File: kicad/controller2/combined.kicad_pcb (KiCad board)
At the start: 2 copper layers, 150.5 x 97.2 mm, 258 parts, among them J1 Conn_01x07_Male, J2 Conn_01x07_Male, J3 Conn_01x07_Male, J4 Conn_01x07_Male, J5V1 Conn_01x01_Male, Q1 BC846B, Q2 IRF3205, Q3 IRF3205, Q4 BC846B, Q5 IRF3205, Q6 IRF3205, U1 BluePill_STM32F103C, U1 LM324, U2 LM324

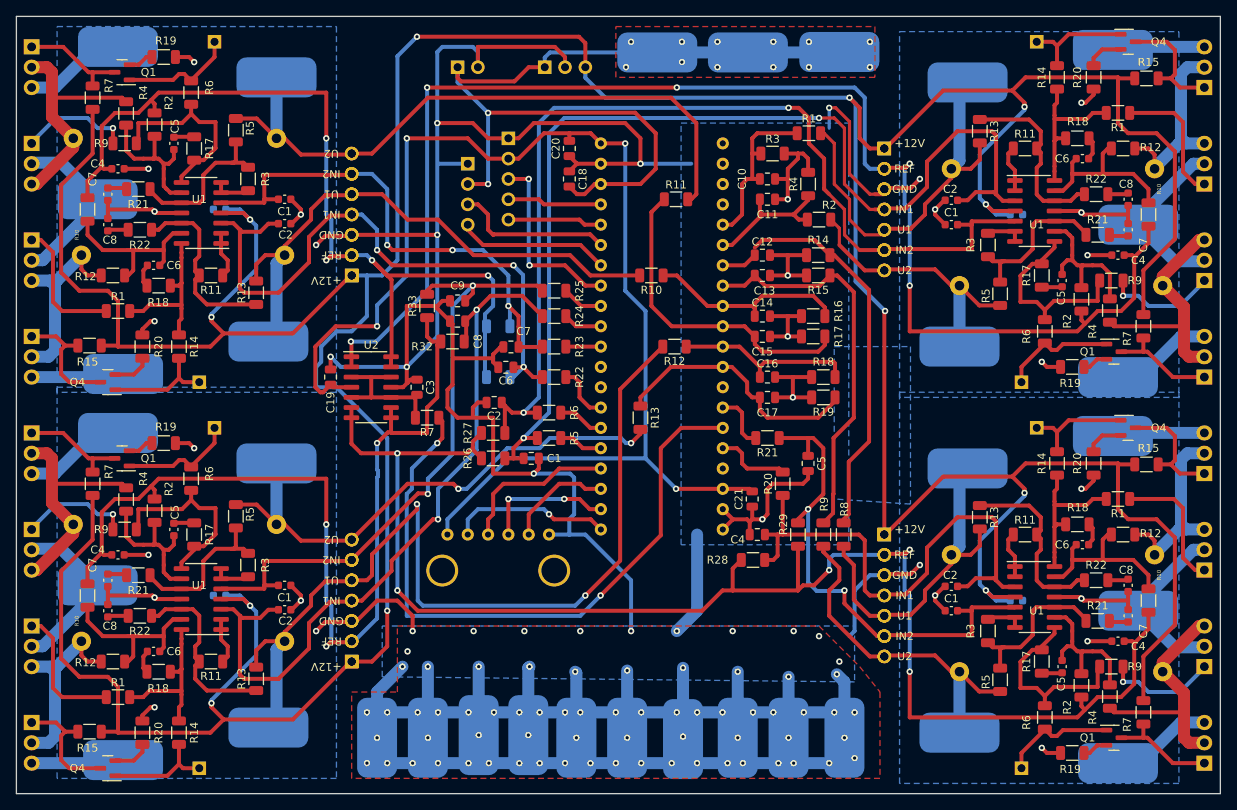
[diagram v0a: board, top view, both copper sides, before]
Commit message: minor schematic cleanups, improve opamp compensation
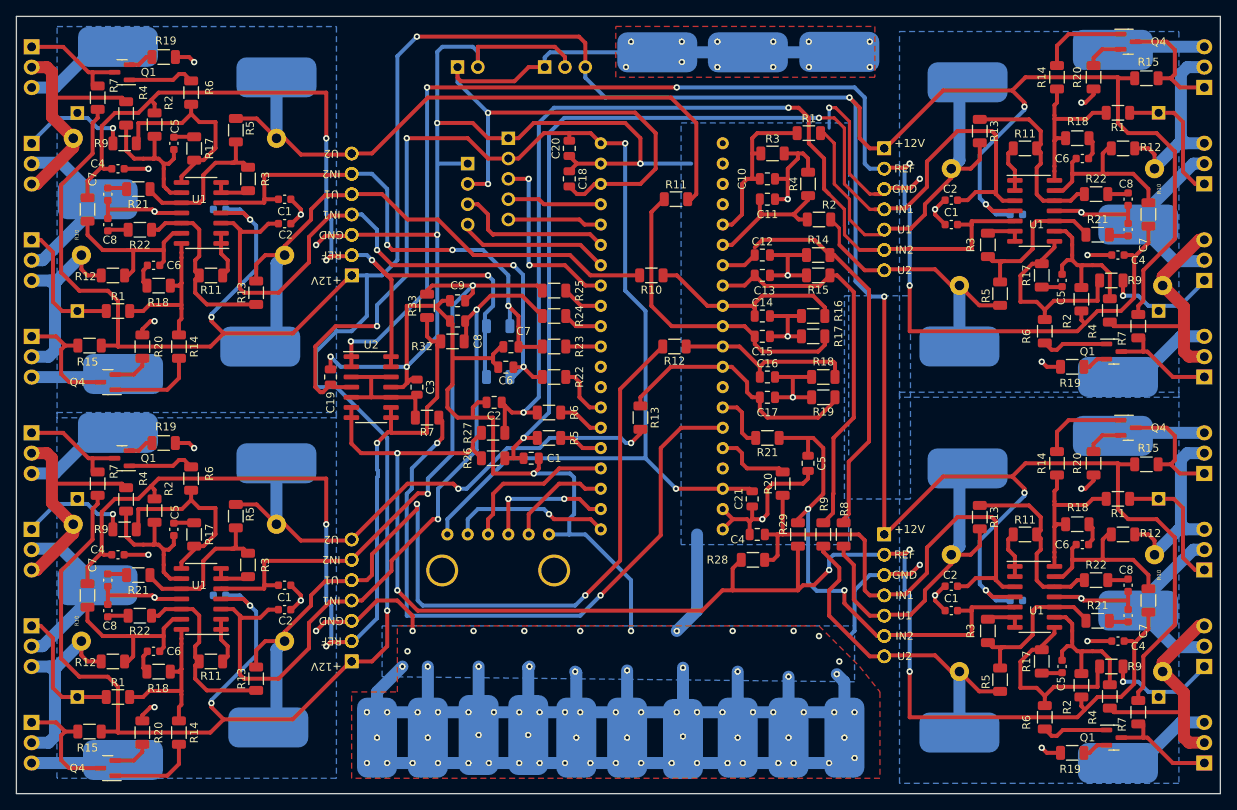
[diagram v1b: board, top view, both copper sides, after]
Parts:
- removed the C1 at (195.0, 120.0)
- removed the C1 at (195.0, 71.8)
- removed the C1 at (142.5, 101.0)
- removed the C1 at (111.6, 116.8)
- removed the C2 at (195.0, 117.0)
- removed the C2 at (137.8, 94.0)
- removed the C2 at (111.6, 119.9)
- removed the C2 at (195.0, 68.7)
- removed the C3 at (128.2, 92.1)
- removed the C3 at (203.1, 70.5)
- removed the C3 at (103.5, 118.1)
- removed the C3 at (203.1, 118.7)
- removed the C4 at (215.8, 75.6)
- removed the C4 at (90.8, 113.0)
- removed the C4 at (170.7, 110.5)
- removed the C4 at (215.8, 123.8)
- removed the C5 at (97.8, 109.9)
- removed the C5 at (208.8, 78.7)
- removed the C5 at (208.8, 127.0)
- removed the C5 at (177.1, 101.6)
- removed the C6 at (139.3, 89.6)
- removed the C6 at (211.4, 63.5)
- removed the C6 at (211.4, 111.8)
- removed the C6 at (95.2, 125.1)
- removed the C7 at (139.9, 87.0)
- removed the C7 at (217.1, 120.6)
- removed the C7 at (217.1, 72.4)
- removed the C7 at (89.5, 116.2)
- removed the C8 at (217.1, 116.8)
- removed the C8 at (89.5, 120.0)
- removed the C8 at (217.1, 68.6)
- removed the C8 at (133.3, 83.8)
- removed the J1 at (186.6, 110.5)
- removed the J1 at (186.6, 62.2) (x2)
- removed the J1 at (120.0, 126.4)
- removed the J5V1 at (218.3, 120.0)
- removed the J5V1 at (88.3, 116.8)
- removed the J5V1 at (218.3, 71.8)
- removed the JBat1 at (109.6, 134.6)
- removed the JBat1 at (109.6, 86.4)
- removed the JBat1 at (197.0, 54.0)
- removed the JBat1 at (197.0, 102.2)
- removed the JBat1 at (127.0, 130.8)
- removed the JBat2 at (196.0, 135.2)
- removed the JBat2 at (196.0, 87.0)
- removed the JBat2 at (110.6, 101.6)
- removed the JBat2 at (138.4, 140.6)
- removed the JGND1 at (215.2, 98.2)
- removed the JGND1 at (215.2, 49.9)
- removed the JGND1 at (91.4, 138.7)
- removed the JGND2 at (90.8, 97.8)
- removed the JGND2 at (215.8, 139.1)
- removed the JGND2 at (215.8, 90.8)
- removed the JTest1 at (101.0, 139.7)
- removed the JTest1 at (101.0, 91.4)
- removed the JTest1 at (205.6, 97.2)
- removed the JTest1 at (205.6, 48.9)
- removed the JTest2 at (102.9, 97.2)
- removed the JTest2 at (102.9, 48.9)
- removed the JTest2 at (203.7, 91.4)
- removed the JTest2 at (203.7, 139.7)
- removed the Q1 at (91.3, 101.0)
- removed the Q1 at (215.3, 135.9)
- removed the Q1 at (215.3, 87.6)
- removed the Q2 at (226.6, 78.7)
- removed the Q2 at (226.6, 127.0)
- removed the Q2 at (80.0, 109.9)
- removed the Q3 at (226.6, 90.8)
- removed the Q3 at (80.0, 97.8)
- removed the Q3 at (226.6, 139.1)
- removed the Q4 at (89.5, 139.7)
- removed the Q4 at (217.1, 97.2)
- removed the Q4 at (217.1, 48.9)
- removed the Q5 at (80.0, 121.9)
- removed the Q5 at (226.6, 66.7)
- removed the Q5 at (226.6, 114.9)
- removed the Q6 at (226.6, 54.6)
- removed the Q6 at (80.0, 134.0)
- removed the Q6 at (226.6, 102.9)
- removed the R1 at (215.8, 57.8)
- removed the R1 at (90.8, 130.8)
- removed the R1 at (177.2, 60.3)
- removed the R1 at (215.8, 106.0)
- removed the R10 at (219.6, 118.7)
- removed the R10 at (157.5, 78.1)
- removed the R10 at (219.6, 70.5)
- removed the R10 at (87.0, 118.1)
- removed the R11 at (204.2, 110.5)
- removed the R11 at (204.2, 62.2)
- removed the R11 at (160.6, 68.6)
- removed the R11 at (102.4, 126.4)
- removed the R12 at (216.4, 110.5)
- removed the R12 at (216.4, 62.2)
- removed the R12 at (160.4, 87.0)
- removed the R12 at (90.2, 126.4)
- removed the R13 at (198.5, 60.1)
- removed the R13 at (156.1, 95.9)
- removed the R13 at (198.5, 108.3)
- removed the R13 at (108.1, 128.5)
- removed the R14 at (98.4, 135.3)
- removed the R14 at (178.3, 75.6)
- removed the R14 at (208.2, 53.3)
- removed the R14 at (208.2, 101.6)
- removed the R15 at (178.3, 78.1)
- removed the R15 at (219.4, 101.7)
- removed the R15 at (87.2, 135.1)
- removed the R15 at (219.4, 53.5)
- removed the R16 at (177.7, 83.2)
- removed the R16 at (86.2, 123.8)
- removed the R16 at (220.4, 113.0)
- removed the R16 at (220.4, 64.8)
- removed the R17 at (206.3, 78.1)
- removed the R17 at (177.7, 85.7)
- removed the R17 at (206.3, 126.4)
- removed the R17 at (100.3, 110.5)
- removed the R18 at (95.9, 127.6)
- removed the R18 at (210.7, 61.0)
- removed the R18 at (210.7, 109.2)
- removed the R18 at (179.0, 90.8)
- removed the R19 at (210.1, 89.5)
- removed the R19 at (210.1, 137.8)
- removed the R19 at (96.5, 99.1)
- removed the R19 at (179.0, 93.3)
- removed the R2 at (178.4, 71.1)
- removed the R2 at (211.2, 129.3)
- removed the R2 at (95.4, 107.5)
- removed the R2 at (211.2, 81.1)
- removed the R20 at (173.9, 104.1)
- removed the R20 at (93.9, 135.3)
- removed the R20 at (212.8, 101.6)
- removed the R20 at (212.8, 53.3)
- removed the R21 at (93.3, 115.6)
- removed the R21 at (172.0, 98.4)
- removed the R21 at (213.3, 121.3)
- removed the R21 at (213.3, 73.0)
- removed the R22 at (213.1, 116.2)
- removed the R22 at (145.3, 90.8)
- removed the R22 at (93.5, 120.7)
- removed the R22 at (213.1, 67.9)
- removed the R3 at (199.5, 74.3)
- removed the R3 at (199.5, 122.5)
- removed the R3 at (107.1, 114.3)
- removed the R3 at (172.6, 62.9)
- removed the R4 at (214.8, 82.5)
- removed the R4 at (91.8, 106.1)
- removed the R4 at (177.1, 66.7)
- removed the R4 at (214.8, 130.7)
- removed the R5 at (105.5, 108.2)
- removed the R5 at (144.7, 98.4)
- removed the R5 at (201.1, 128.6)
- removed the R5 at (201.1, 80.4)
- removed the R6 at (99.9, 103.5)
- removed the R6 at (206.7, 133.3)
- removed the R6 at (206.7, 85.1)
- removed the R6 at (144.7, 95.2)
- removed the R7 at (87.6, 104.1)
- removed the R7 at (219.0, 132.7)
- removed the R7 at (219.0, 84.5)
- removed the R7 at (129.4, 95.9)
- removed the R7 at (87.6, 55.9)
- removed the R8 at (181.5, 110.5)
- removed the R8 at (85.2, 109.2)
- removed the R8 at (221.4, 127.6)
- removed the R8 at (221.4, 79.4)
- removed the R9 at (215.0, 78.7)
- removed the R9 at (179.0, 110.5)
- removed the R9 at (215.0, 127.0)
- removed the R9 at (91.6, 109.9)
- removed the U1 at (101.2, 118.6)
- removed the U1 at (205.4, 118.3)
- removed the U1 at (205.4, 70.0)
- removed the U1 at (158.8, 85.7)
- added C1: 1u, Capacitor_SMD:C_0603_1608Metric, F.Cu at (195.0, 71.7)
- added C1: 1u, Capacitor_SMD:C_0603_1608Metric, F.Cu at (195.0, 120.0)
- added C1: C, Capacitor_SMD:C_0805_2012Metric, F.Cu at (142.5, 101.0)
- added C1: 1u, Capacitor_SMD:C_0603_1608Metric, F.Cu at (111.6, 116.8)
- added C2: 1u, Capacitor_SMD:C_0603_1608Metric, F.Cu at (195.0, 68.7)
- added C2: 1u, Capacitor_SMD:C_0603_1608Metric, F.Cu at (195.0, 116.9)
- added C2: 1u, Capacitor_SMD:C_0603_1608Metric, F.Cu at (111.6, 119.9)
- added C2: C, Capacitor_SMD:C_0805_2012Metric, F.Cu at (137.8, 94.0)
- added C3: C, Capacitor_SMD:C_0805_2012Metric, F.Cu at (128.2, 92.1)
- added C3: 1u, Capacitor_SMD:C_0603_1608Metric, B.Cu at (203.1, 70.5)
- added C3: 1u, Capacitor_SMD:C_0603_1608Metric, B.Cu at (103.5, 118.1)
- added C3: 1u, Capacitor_SMD:C_0603_1608Metric, B.Cu at (203.1, 118.7)
- added C4: 1u, Capacitor_SMD:C_0603_1608Metric, F.Cu at (90.8, 113.0)
- added C4: 1u, Capacitor_SMD:C_0603_1608Metric, F.Cu at (215.8, 75.6)
- added C4: 1u, Capacitor_SMD:C_0603_1608Metric, F.Cu at (215.8, 123.8)
- added C4: C, Capacitor_SMD:C_0805_2012Metric, F.Cu at (170.7, 110.5)
- added C5: 1u, Capacitor_SMD:C_0603_1608Metric, F.Cu at (97.8, 109.8)
- added C5: 1u, Capacitor_SMD:C_0603_1608Metric, F.Cu at (208.8, 127.0)
- added C5: C, Capacitor_SMD:C_0805_2012Metric, F.Cu at (177.1, 101.6)
- added C5: 1u, Capacitor_SMD:C_0603_1608Metric, F.Cu at (208.8, 78.7)
- added C6: 1u, Capacitor_SMD:C_0603_1608Metric, F.Cu at (211.4, 63.5)
- added C6: C, Capacitor_SMD:C_0805_2012Metric, F.Cu at (139.3, 89.6)
- added C6: 1u, Capacitor_SMD:C_0603_1608Metric, F.Cu at (211.4, 111.7)
- added C6: 1u, Capacitor_SMD:C_0603_1608Metric, F.Cu at (95.2, 125.1)
- added C7: 1u, Capacitor_SMD:C_0603_1608Metric, F.Cu at (217.1, 120.6)
- added C7: C, Capacitor_SMD:C_0805_2012Metric, F.Cu at (139.9, 87.0)
- added C7: 1u, Capacitor_SMD:C_0603_1608Metric, F.Cu at (89.5, 116.2)
- added C7: 1u, Capacitor_SMD:C_0603_1608Metric, F.Cu at (217.1, 72.4)
- added C8: 1u, Capacitor_SMD:C_0603_1608Metric, F.Cu at (217.1, 116.8)
- added C8: 1u, Capacitor_SMD:C_0603_1608Metric, F.Cu at (217.1, 68.6)
- added C8: 1u, Capacitor_SMD:C_0603_1608Metric, F.Cu at (89.5, 120.0)
- added C8: C, Capacitor_SMD:C_0805_2012Metric, F.Cu at (133.2, 83.8)
- added J1: Conn_01x07_Male, Connector_PinHeader_2.54mm:PinHeader_1x07_P2.54mm_Vertical, B.Cu at (186.6, 110.5)
- added J1 (x2): Conn_01x07_Male, Connector_PinHeader_2.54mm:PinHeader_1x07_P2.54mm_Vertical, B.Cu at (186.6, 62.2)
- added J1: Conn_01x07_Male, Connector_PinHeader_2.54mm:PinHeader_1x07_P2.54mm_Vertical, B.Cu at (120.0, 126.4)
- added J5V1: Conn_01x01_Male, Channel:PowerPad, B.Cu at (218.3, 71.7)
- added J5V1: Conn_01x01_Male, Channel:PowerPad, B.Cu at (218.3, 120.0)
- added J5V1: Conn_01x01_Male, Channel:PowerPad, B.Cu at (88.3, 116.8)
- added JBat1: Conn_01x01_Male, controller:PowerPin, B.Cu at (127.0, 130.8)
- added JBat1: Conn_01x01_Male, Channel:PowerPad, B.Cu at (197.0, 54.0)
- added JBat1: Conn_01x01_Male, Channel:PowerPad, B.Cu at (108.6, 87.0)
- added JBat1: Conn_01x01_Male, Channel:PowerPad, B.Cu at (109.6, 134.6)
- added JBat1: Conn_01x01_Male, Channel:PowerPad, B.Cu at (197.0, 102.2)
- added JBat2: Conn_01x01_Male, controller:PowerPin, B.Cu at (138.4, 140.6)
- added JBat2: Conn_01x01_Male, Channel:PowerPad, B.Cu at (196.0, 135.2)
- added JBat2: Conn_01x01_Male, Channel:PowerPad, B.Cu at (196.0, 87.0)
- added JBat2: Conn_01x01_Male, Channel:PowerPad, B.Cu at (110.6, 101.6)
- added JGND1: Conn_01x01_Male, Channel:PowerPad, B.Cu at (91.4, 138.7)
- added JGND1: Conn_01x01_Male, Channel:PowerPad, B.Cu at (215.2, 49.9)
- added JGND1: Conn_01x01_Male, Channel:PowerPad, B.Cu at (215.2, 98.2)
- added JGND2: Conn_01x01_Male, Channel:PowerPad, B.Cu at (90.8, 97.8)
- added JGND2: Conn_01x01_Male, Channel:PowerPad, B.Cu at (215.8, 139.0)
- added JGND2: Conn_01x01_Male, Channel:PowerPad, B.Cu at (215.8, 90.8)
- added JTest1: Conn_01x01_Male, Connector_PinHeader_2.54mm:PinHeader_1x01_P2.54mm_Vertical, B.Cu at (220.9, 106.0)
- added JTest1: Conn_01x01_Male, Connector_PinHeader_2.54mm:PinHeader_1x01_P2.54mm_Vertical, B.Cu at (220.9, 57.8)
- added JTest1: Conn_01x01_Male, Connector_PinHeader_2.54mm:PinHeader_1x01_P2.54mm_Vertical, B.Cu at (85.7, 82.5)
- added JTest1: Conn_01x01_Male, Connector_PinHeader_2.54mm:PinHeader_1x01_P2.54mm_Vertical, B.Cu at (85.7, 130.8)
- added JTest2: Conn_01x01_Male, Connector_PinHeader_2.54mm:PinHeader_1x01_P2.54mm_Vertical, B.Cu at (220.9, 82.5)
- added JTest2: Conn_01x01_Male, Connector_PinHeader_2.54mm:PinHeader_1x01_P2.54mm_Vertical, B.Cu at (85.7, 57.8)
- added JTest2: Conn_01x01_Male, Connector_PinHeader_2.54mm:PinHeader_1x01_P2.54mm_Vertical, B.Cu at (85.7, 106.0)
- added JTest2: Conn_01x01_Male, Connector_PinHeader_2.54mm:PinHeader_1x01_P2.54mm_Vertical, B.Cu at (220.9, 130.8)
- added Q1: BC846B, Package_TO_SOT_SMD:SOT-23, F.Cu at (215.3, 87.6)
- added Q1: BC846B, Package_TO_SOT_SMD:SOT-23, F.Cu at (91.3, 101.0)
- added Q1: BC846B, Package_TO_SOT_SMD:SOT-23, F.Cu at (215.3, 135.9)
- added Q2: IRF3205, Package_TO_SOT_THT:TO-220-3_Vertical, B.Cu at (80.0, 109.8)
- added Q2: IRF3205, Package_TO_SOT_THT:TO-220-3_Vertical, B.Cu at (226.6, 127.0)
- added Q2: IRF3205, Package_TO_SOT_THT:TO-220-3_Vertical, B.Cu at (226.6, 78.7)
- added Q3: IRF3205, Package_TO_SOT_THT:TO-220-3_Vertical, B.Cu at (80.0, 97.8)
- added Q3: IRF3205, Package_TO_SOT_THT:TO-220-3_Vertical, B.Cu at (226.6, 90.8)
- added Q3: IRF3205, Package_TO_SOT_THT:TO-220-3_Vertical, B.Cu at (226.6, 139.0)
- added Q4: BC846B, Package_TO_SOT_SMD:SOT-23, F.Cu at (217.1, 48.9)
- added Q4: BC846B, Package_TO_SOT_SMD:SOT-23, F.Cu at (217.1, 97.1)
- added Q4: BC846B, Package_TO_SOT_SMD:SOT-23, F.Cu at (89.5, 139.7)
- added Q5: IRF3205, Package_TO_SOT_THT:TO-220-3_Vertical, B.Cu at (226.6, 66.7)
- added Q5: IRF3205, Package_TO_SOT_THT:TO-220-3_Vertical, B.Cu at (226.6, 114.9)
- added Q5: IRF3205, Package_TO_SOT_THT:TO-220-3_Vertical, B.Cu at (80.0, 121.9)
- added Q6: IRF3205, Package_TO_SOT_THT:TO-220-3_Vertical, B.Cu at (226.6, 102.9)
- added Q6: IRF3205, Package_TO_SOT_THT:TO-220-3_Vertical, B.Cu at (226.6, 54.6)
- added Q6: IRF3205, Package_TO_SOT_THT:TO-220-3_Vertical, B.Cu at (80.0, 134.0)
- added R1: 1k, Resistor_SMD:R_1206_3216Metric, F.Cu at (215.8, 106.0)
- added R1: 1k, Resistor_SMD:R_1206_3216Metric, F.Cu at (90.8, 130.8)
- added R1: 1k, Resistor_SMD:R_1206_3216Metric, F.Cu at (215.8, 57.8)
- added R1: 10k, Resistor_SMD:R_1206_3216Metric, F.Cu at (177.2, 60.3)
- added R10: 10k, Resistor_SMD:R_1206_3216Metric, F.Cu at (157.5, 78.1)
- added R10: 22k, Resistor_SMD:R_1206_3216Metric, F.Cu at (219.6, 118.7)
- added R10: 22k, Resistor_SMD:R_1206_3216Metric, F.Cu at (219.6, 70.5)
- added R10: 22k, Resistor_SMD:R_1206_3216Metric, F.Cu at (87.0, 118.1)
- added R11: 22k, Resistor_SMD:R_1206_3216Metric, F.Cu at (102.4, 126.4)
- added R11: 22k, Resistor_SMD:R_1206_3216Metric, F.Cu at (204.2, 62.2)
- added R11: 22k, Resistor_SMD:R_1206_3216Metric, F.Cu at (204.2, 110.5)
- added R11: 10k, Resistor_SMD:R_1206_3216Metric, F.Cu at (160.6, 68.6)
- added R12: 10k, Resistor_SMD:R_1206_3216Metric, F.Cu at (216.4, 62.2)
- added R12: 10k, Resistor_SMD:R_1206_3216Metric, F.Cu at (216.4, 110.5)
- added R12: 10k, Resistor_SMD:R_1206_3216Metric, F.Cu at (160.4, 87.0)
- added R12: 10k, Resistor_SMD:R_1206_3216Metric, F.Cu at (90.2, 126.4)
- added R13: 10k, Resistor_SMD:R_1206_3216Metric, F.Cu at (156.1, 95.9)
- added R13: 10k, Resistor_SMD:R_1206_3216Metric, F.Cu at (198.5, 60.1)
- added R13: 10k, Resistor_SMD:R_1206_3216Metric, F.Cu at (198.5, 108.3)
- added R13: 10k, Resistor_SMD:R_1206_3216Metric, F.Cu at (108.1, 128.5)
- added R14: 22k, Resistor_SMD:R_1206_3216Metric, F.Cu at (208.2, 101.6)
- added R14: 22k, Resistor_SMD:R_1206_3216Metric, F.Cu at (208.2, 53.3)
- added R14: 22k, Resistor_SMD:R_1206_3216Metric, F.Cu at (98.4, 135.2)
- added R14: 10k, Resistor_SMD:R_1206_3216Metric, F.Cu at (178.3, 75.6)
- added R15: 22k, Resistor_SMD:R_1206_3216Metric, F.Cu at (87.2, 135.1)
- added R15: 22k, Resistor_SMD:R_1206_3216Metric, F.Cu at (219.4, 53.5)
- added R15: 22k, Resistor_SMD:R_1206_3216Metric, F.Cu at (219.4, 101.7)
- added R15: 10k, Resistor_SMD:R_1206_3216Metric, F.Cu at (178.3, 78.1)
- added R16: 10k, Resistor_SMD:R_1206_3216Metric, F.Cu at (177.7, 83.2)
- added R16: 0.22, Resistor_THT:R_Axial_DIN0617_L17.0mm_D6.0mm_P25.40mm_Horizontal, B.Cu at (220.4, 113.0)
- added R16: 0.22, Resistor_THT:R_Axial_DIN0617_L17.0mm_D6.0mm_P25.40mm_Horizontal, B.Cu at (86.2, 123.8)
- added R16: 0.22, Resistor_THT:R_Axial_DIN0617_L17.0mm_D6.0mm_P25.40mm_Horizontal, B.Cu at (220.4, 64.8)
- added R17: 1k, Resistor_SMD:R_1206_3216Metric, F.Cu at (100.3, 110.5)
- added R17: 10k, Resistor_SMD:R_1206_3216Metric, F.Cu at (177.7, 85.7)
- added R17: 1k, Resistor_SMD:R_1206_3216Metric, F.Cu at (206.3, 78.1)
- added R17: 1k, Resistor_SMD:R_1206_3216Metric, F.Cu at (206.3, 126.3)
- added R18: 1k, Resistor_SMD:R_1206_3216Metric, F.Cu at (210.7, 109.2)
- added R18: 1k, Resistor_SMD:R_1206_3216Metric, F.Cu at (95.9, 127.6)
- added R18: 1k, Resistor_SMD:R_1206_3216Metric, F.Cu at (210.7, 60.9)
- added R18: 10k, Resistor_SMD:R_1206_3216Metric, F.Cu at (179.0, 90.8)
- added R19: 1k, Resistor_SMD:R_1206_3216Metric, F.Cu at (96.5, 99.0)
- added R19: 1k, Resistor_SMD:R_1206_3216Metric, F.Cu at (210.1, 137.8)
- added R19: 1k, Resistor_SMD:R_1206_3216Metric, F.Cu at (210.1, 89.5)
- added R19: 10k, Resistor_SMD:R_1206_3216Metric, F.Cu at (179.0, 93.3)
- added R2: 22k, Resistor_SMD:R_1206_3216Metric, F.Cu at (211.2, 81.1)
- added R2: 10k, Resistor_SMD:R_1206_3216Metric, F.Cu at (178.4, 71.1)
- added R2: 22k, Resistor_SMD:R_1206_3216Metric, F.Cu at (95.4, 107.5)
- added R2: 22k, Resistor_SMD:R_1206_3216Metric, F.Cu at (211.2, 129.3)
- added R20: 1k, Resistor_SMD:R_1206_3216Metric, F.Cu at (93.8, 135.2)
- added R20: 1k, Resistor_SMD:R_1206_3216Metric, F.Cu at (212.8, 53.3)
- added R20: 1k, Resistor_SMD:R_1206_3216Metric, F.Cu at (212.8, 101.6)
- added R20: 10k, Resistor_SMD:R_1206_3216Metric, F.Cu at (173.9, 104.1)
- added R21: 1k, Resistor_SMD:R_1206_3216Metric, F.Cu at (213.3, 73.0)
- added R21: 1k, Resistor_SMD:R_1206_3216Metric, F.Cu at (213.3, 121.3)
- added R21: 10k, Resistor_SMD:R_1206_3216Metric, F.Cu at (172.0, 98.4)
- added R21: 1k, Resistor_SMD:R_1206_3216Metric, F.Cu at (93.3, 115.6)
- added R22: 10k, Resistor_SMD:R_1206_3216Metric, F.Cu at (145.3, 90.8)
- added R22: 1k, Resistor_SMD:R_1206_3216Metric, F.Cu at (213.1, 116.2)
- added R22: 1k, Resistor_SMD:R_1206_3216Metric, F.Cu at (213.1, 67.9)
- added R22: 1k, Resistor_SMD:R_1206_3216Metric, F.Cu at (93.5, 120.6)
- added R3: 22k, Resistor_SMD:R_1206_3216Metric, F.Cu at (199.5, 122.5)
- added R3: 10k, Resistor_SMD:R_1206_3216Metric, F.Cu at (172.6, 62.9)
- added R3: 22k, Resistor_SMD:R_1206_3216Metric, F.Cu at (107.1, 114.3)
- added R3: 22k, Resistor_SMD:R_1206_3216Metric, F.Cu at (199.5, 74.3)
- added R4: 10k, Resistor_SMD:R_1206_3216Metric, F.Cu at (177.1, 66.7)
- added R4: 10k, Resistor_SMD:R_1206_3216Metric, F.Cu at (214.8, 130.7)
- added R4: 10k, Resistor_SMD:R_1206_3216Metric, F.Cu at (91.8, 106.1)
- added R4: 10k, Resistor_SMD:R_1206_3216Metric, F.Cu at (214.8, 82.5)
- added R5: 10k, Resistor_SMD:R_1206_3216Metric, F.Cu at (201.1, 128.6)
- added R5: 10k, Resistor_SMD:R_1206_3216Metric, F.Cu at (105.5, 108.2)
- added R5: 10k, Resistor_SMD:R_1206_3216Metric, F.Cu at (201.1, 80.4)
- added R5: 10k, Resistor_SMD:R_1206_3216Metric, F.Cu at (144.7, 98.4)
- added R6: 22k, Resistor_SMD:R_1206_3216Metric, F.Cu at (206.7, 85.1)
- added R6: 22k, Resistor_SMD:R_1206_3216Metric, F.Cu at (99.9, 103.5)
- added R6: 10k, Resistor_SMD:R_1206_3216Metric, F.Cu at (144.7, 95.2)
- added R6: 22k, Resistor_SMD:R_1206_3216Metric, F.Cu at (206.7, 133.3)
- added R7: 22k, Resistor_SMD:R_1206_3216Metric, F.Cu at (88.3, 104.1)
- added R7: 22k, Resistor_SMD:R_1206_3216Metric, F.Cu at (88.3, 55.9)
- added R7: 22k, Resistor_SMD:R_1206_3216Metric, F.Cu at (218.3, 84.4)
- added R7: 10k, Resistor_SMD:R_1206_3216Metric, F.Cu at (129.4, 95.9)
- added R7: 22k, Resistor_SMD:R_1206_3216Metric, F.Cu at (218.3, 132.7)
- added R8: 10k, Resistor_SMD:R_1206_3216Metric, F.Cu at (181.5, 110.5)
- added R8: 0.22, Resistor_THT:R_Axial_DIN0617_L17.0mm_D6.0mm_P25.40mm_Horizontal, B.Cu at (221.4, 127.6)
- added R8: 0.22, Resistor_THT:R_Axial_DIN0617_L17.0mm_D6.0mm_P25.40mm_Horizontal, B.Cu at (221.4, 79.4)
- added R8: 0.22, Resistor_THT:R_Axial_DIN0617_L17.0mm_D6.0mm_P25.40mm_Horizontal, B.Cu at (85.2, 109.2)
- added R9: 1k, Resistor_SMD:R_1206_3216Metric, F.Cu at (215.0, 127.0)
- added R9: 10k, Resistor_SMD:R_1206_3216Metric, F.Cu at (179.0, 110.5)
- added R9: 1k, Resistor_SMD:R_1206_3216Metric, F.Cu at (91.6, 109.8)
- added R9: 1k, Resistor_SMD:R_1206_3216Metric, F.Cu at (215.0, 78.7)
- added U1: LM324, Package_SO:SOIC-14_3.9x8.7mm_P1.27mm, F.Cu at (205.4, 118.3)
- added U1: LM324, Package_SO:SOIC-14_3.9x8.7mm_P1.27mm, F.Cu at (101.2, 118.5)
- added U1: LM324, Package_SO:SOIC-14_3.9x8.7mm_P1.27mm, F.Cu at (205.4, 70.0)
- added U1: BluePill_STM32F103C, controller:BluePill, B.Cu at (158.8, 85.7)
- R14, R15, R6: value 10k -> 22k
- R17, R18, R21, R22: value 22k -> 1k
- R19, R20: value 2.2k -> 1k
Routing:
- net (no net): track 1248.6 -> 1215.7 mm
- net +12V: track 605.7 -> 607.8 mm
